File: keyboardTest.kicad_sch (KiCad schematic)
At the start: 4 parts, among them J1 COCO_CONNECTION, J1 DRAGON_CONNECTION

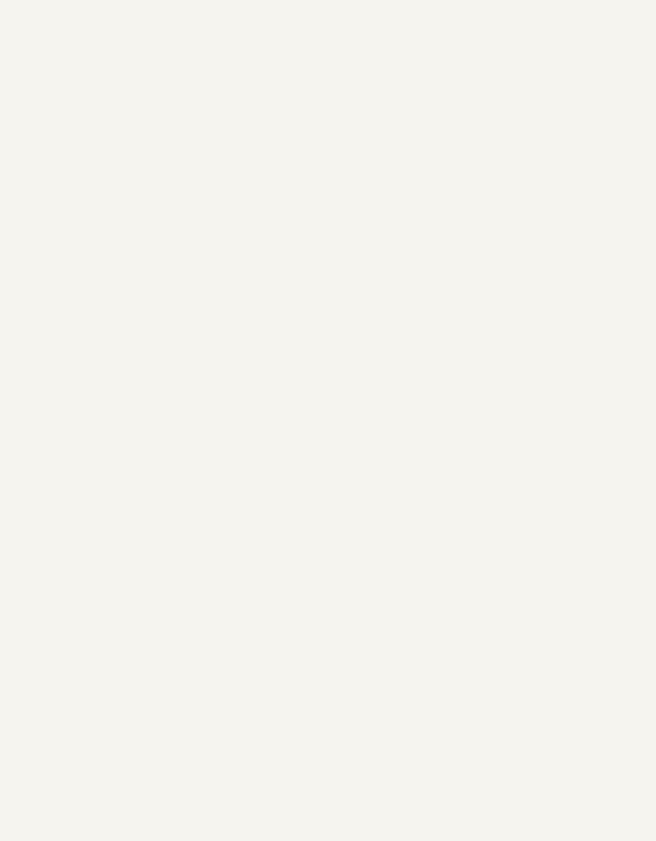
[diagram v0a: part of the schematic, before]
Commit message: add pico for hid
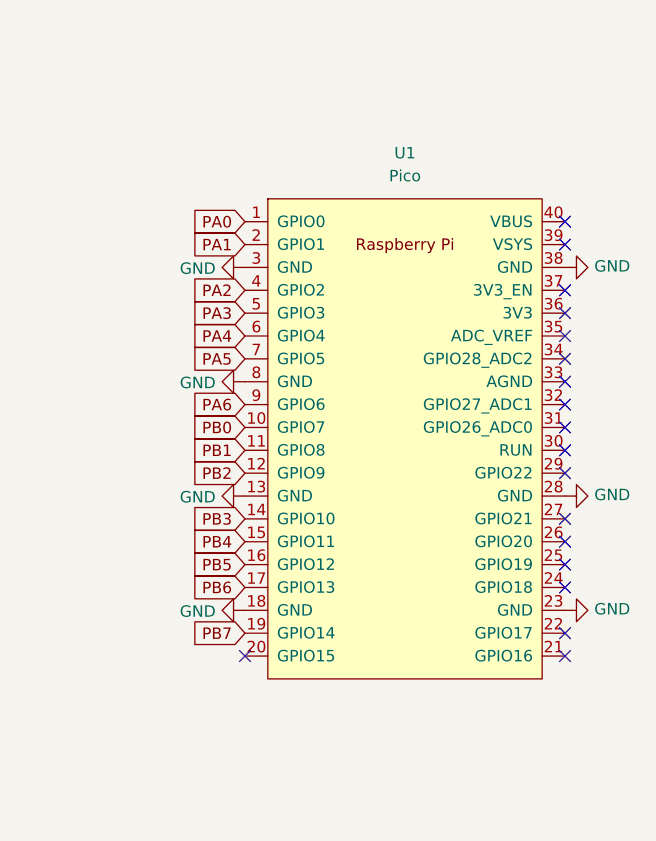
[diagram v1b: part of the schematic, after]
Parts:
- added U1: Pico, pico:RPi_Pico_SMD_TH, symbol pico:Pico
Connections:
- net GND: now also U1.13 (GND), U1.18 (GND), U1.23 (GND), U1.28 (GND), U1.3 (GND), U1.38 (GND), U1.8 (GND)
- net PA0: now also U1.1 (GPIO0)
- net PA1: now also U1.2 (GPIO1)
- net PA2: now also U1.4 (GPIO2)
- net PA3: now also U1.5 (GPIO3)
- net PA4: now also U1.6 (GPIO4)
- net PA5: now also U1.7 (GPIO5)
- net PA6: now also U1.9 (GPIO6)
- net PB0: now also U1.10 (GPIO7)
- net PB1: now also U1.11 (GPIO8)
- net PB2: now also U1.12 (GPIO9)
- net PB3: now also U1.14 (GPIO10)
- net PB4: now also U1.15 (GPIO11)
- net PB5: now also U1.16 (GPIO12)
- net PB6: now also U1.17 (GPIO13)
- net PB7: now also U1.19 (GPIO14)
- no-connect marks 0 -> 18

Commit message: update board mounting
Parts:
- added H10, H11, H3, H4, H5, H6, H7, H8, H9: MountingHole, MountingHole:MountingHole_3.2mm_M3, symbol Mechanical:MountingHole
- H1, H2: now left out of the parts list
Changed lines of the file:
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@@
+    )
+  )
+  (symbol (lib_id "Mechanical:MountingHole") (at 31.75 163.83 0) (unit 1)
+    (in_bom no) (on_board yes) (dnp yes) (fields_autoplaced)
+    (property "Reference" "H3" (at 34.29 163.195 0)
+      (effects (font (size 1.27 1.27)) (justify left))
+    )
+    (property "Value" "MountingHole" (at 34.29 165.735 0)
+      (effects (font (size 1.27 1.27)) (justify left))
+    )
+    (property "Footprint" "MountingHole:MountingHole_3.2mm_M3" (at 31.75 163.83 0)
+      (effects (font (size 1.27 1.27)) hide)
+    )
+    (property "Datasheet" "~" (at 31.75 163.83 0)
+      (effects (font (size 1.27 1.27)) hide)
+    )
+    (instances
+      (project "keyboardTest"
+        (path "/f35e9616-f481-4cdb-9e32-caf70bd322dd"
+          (reference "H3") (unit 1)
+        )
+      )
+    )
+  )
+  (symbol (lib_id "Mechanical:MountingHole") (at 60.96 178.562 0) (unit 1)
+    (in_bom no) (on_board yes) (dnp yes) (fields_autoplaced)
+    (property "Reference" "H6" (at 63.5 177.927 0)
+      (effects (font (size 1.27 1.27)) (justify left))
+    )
+    (property "Value" "MountingHole" (at 63.5 180.467 0)
+      (effects (font (size 1.27 1.27)) (justify left))
+    )
+    (property "Footprint" "MountingHole:MountingHole_3.2mm_M3" (at 60.96 178.562 0)
+      (effects (font (size 1.27 1.27)) hide)
+    )
+    (property "Datasheet" "~" (at 60.96 178.562 0)
+      (effects (font (size 1.27 1.27)) hide)
+    )
+    (instances
+      (project "keyboardTest"
+        (path "/f35e9616-f481-4cdb-9e32-caf70bd322dd"
+          (reference "H6") (unit 1)
+        )
+      )
+    )
+  )
+  (symbol (lib_id "Mechanical:MountingHole") (at 90.17 192.278 0) (unit 1)
+    (in_bom no) (on_board yes) (dnp yes) (fields_autoplaced)
+    (property "Reference" "H11" (at 92.71 191.643 0)
+      (effects (font (size 1.27 1.27)) (justify left))
+    )
+    (property "Value" "MountingHole" (at 92.71 194.183 0)
+      (effects (font (size 1.27 1.27)) (justify left))
+    )
+    (property "Footprint" "MountingHole:MountingHole_3.2mm_M3" (at 90.17 192.278 0)
+      (effects (font (size 1.27 1.27)) hide)
+    )
+    (property "Datasheet" "~" (at 90.17 192.278 0)
+      (effects (font (size 1.27 1.27)) hide)
+    )
+    (instances
+      (project "keyboardTest"
+        (path "/f35e9616-f481-4cdb-9e32-caf70bd322dd"
+          (reference "H11") (unit 1)
+        )
+      )
     )
   )
@@
         (path "/f35e9616-f481-4cdb-9e32-caf70bd322dd"
           (reference "#PWR03") (unit 1)
+        )
+      )
+    )
+  )
+  (symbol (lib_id "Mechanical:MountingHole") (at 32.766 177.546 0) (unit 1)
+    (in_bom no) (on_board yes) (dnp yes) (fields_autoplaced)
+    (property "Reference" "H4" (at 35.306 176.911 0)
+      (effects (font (size 1.27 1.27)) (justify left))
+    )
+    (property "Value" "MountingHole" (at 35.306 179.451 0)
+      (effects (font (size 1.27 1.27)) (justify left))
+    )
+    (property "Footprint" "MountingHole:MountingHole_3.2mm_M3" (at 32.766 177.546 0)
+      (effects (font (size 1.27 1.27)) hide)
+    )
+    (property "Datasheet" "~" (at 32.766 177.546 0)
+      (effects (font (size 1.27 1.27)) hide)
+    )
+    (instances
+      (project "keyboardTest"
+        (path "/f35e9616-f481-4cdb-9e32-caf70bd322dd"
+          (reference "H4") (unit 1)
         )
       )
@@
   )
   (symbol (lib_id "Mechanical:MountingHole") (at 59.69 132.588 0) (unit 1)
-    (in_bom yes) (on_board yes) (dnp no) (fields_autoplaced)
+    (in_bom no) (on_board yes) (dnp no) (fields_autoplaced)
     (property "Reference" "H1" (at 62.23 131.953 0)
       (effects (font (size 1.27 1.27)) (justify left))
@@
         (path "/f35e9616-f481-4cdb-9e32-caf70bd322dd"
           (reference "H1") (unit 1)
+        )
+      )
+    )
+  )
+  (symbol (lib_id "Mechanical:MountingHole") (at 89.3819 164.2902 0) (unit 1)
+    (in_bom no) (on_board yes) (dnp yes) (fields_autoplaced)
+    (property "Reference" "H9" (at 91.9219 163.6552 0)
+      (effects (font (size 1.27 1.27)) (justify left))
+    )
+    (property "Value" "MountingHole" (at 91.9219 166.1952 0)
+      (effects (font (size 1.27 1.27)) (justify left))
+    )
+    (property "Footprint" "MountingHole:MountingHole_3.2mm_M3" (at 89.3819 164.2902 0)
+      (effects (font (size 1.27 1.27)) hide)
+    )
+    (property "Datasheet" "~" (at 89.3819 164.2902 0)
+      (effects (font (size 1.27 1.27)) hide)
+    )
+    (instances
+      (project "keyboardTest"
+        (path "/f35e9616-f481-4cdb-9e32-caf70bd322dd"
+          (reference "H9") (unit 1)
+        )
+      )
+    )
+  )
+  (symbol (lib_id "Mechanical:MountingHole") (at 89.662 178.308 0) (unit 1)
+    (in_bom no) (on_board yes) (dnp yes) (fields_autoplaced)
+    (property "Reference" "H10" (at 92.202 177.673 0)
+      (effects (font (size 1.27 1.27)) (justify left))
+    )
+    (property "Value" "MountingHole" (at 92.202 180.213 0)
+      (effects (font (size 1.27 1.27)) (justify left))
+    )
+    (property "Footprint" "MountingHole:MountingHole_3.2mm_M3" (at 89.662 178.308 0)
+      (effects (font (size 1.27 1.27)) hide)
+    )
+    (property "Datasheet" "~" (at 89.662 178.308 0)
+      (effects (font (size 1.27 1.27)) hide)
+    )
+    (instances
+      (project "keyboardTest"
+        (path "/f35e9616-f481-4cdb-9e32-caf70bd322dd"
+          (reference "H10") (unit 1)
         )
       )
@@
     )
   )
+  (symbol (lib_id "Mechanical:MountingHole") (at 61.468 193.548 0) (unit 1)
+    (in_bom no) (on_board yes) (dnp yes) (fields_autoplaced)
+    (property "Reference" "H8" (at 64.008 192.913 0)
+      (effects (font (size 1.27 1.27)) (justify left))
+    )
+    (property "Value" "MountingHole" (at 64.008 195.453 0)
+      (effects (font (size 1.27 1.27)) (justify left))
+    )
+    (property "Footprint" "MountingHole:MountingHole_3.2mm_M3" (at 61.468 193.548 0)
+      (effects (font (size 1.27 1.27)) hide)
+    )
+    (property "Datasheet" "~" (at 61.468 193.548 0)
+      (effects (font (size 1.27 1.27)) hide)
+    )
+    (instances
+      (project "keyboardTest"
+        (path "/f35e9616-f481-4cdb-9e32-caf70bd322dd"
+          (reference "H8") (unit 1)
+        )
+      )
+    )
+  )
   (symbol (lib_id "power:GND") (at 199.39 106.68 90) (unit 1)
     (in_bom yes) (on_board yes) (dnp no)
@@
         (path "/f35e9616-f481-4cdb-9e32-caf70bd322dd"
           (reference "#PWR08") (unit 1)
+        )
+      )
+    )
+  )
+  (symbol (lib_id "Mechanical:MountingHole") (at 61.214 163.576 0) (unit 1)
+    (in_bom no) (on_board yes) (dnp yes) (fields_autoplaced)
+    (property "Reference" "H7" (at 63.754 162.941 0)
+      (effects (font (size 1.27 1.27)) (justify left))
+    )
+    (property "Value" "MountingHole" (at 63.754 165.481 0)
+      (effects (font (size 1.27 1.27)) (justify left))
+    )
+    (property "Footprint" "MountingHole:MountingHole_3.2mm_M3" (at 61.214 163.576 0)
+      (effects (font (size 1.27 1.27)) hide)
+    )
+    (property "Datasheet" "~" (at 61.214 163.576 0)
+      (effects (font (size 1.27 1.27)) hide)
+    )
+    (instances
+      (project "keyboardTest"
+        (path "/f35e9616-f481-4cdb-9e32-caf70bd322dd"
+          (reference "H7") (unit 1)
         )
       )
@@
   )
   (symbol (lib_id "Mechanical:MountingHole") (at 59.69 146.304 0) (unit 1)
-    (in_bom yes) (on_board yes) (dnp no) (fields_autoplaced)
+    (in_bom no) (on_board yes) (dnp no) (fields_autoplaced)
     (property "Reference" "H2" (at 62.23 145.669 0)
       (effects (font (size 1.27 1.27)) (justify left))
@@
         )
       )
+    )
+  )
+  (symbol (lib_id "Mechanical:MountingHole") (at 33.02 193.04 0) (unit 1)
+    (in_bom no) (on_board yes) (dnp yes) (fields_autoplaced)
+    (property "Reference" "H5" (at 35.56 192.405 0)
+      (effects (font (size 1.27 1.27)) (justify left))
+    )
+    (property "Value" "MountingHole" (at 35.56 194.945 0)
+      (effects (font (size 1.27 1.27)) (justify left))
+    )
+    (property "Footprint" "MountingHole:MountingHole_3.2mm_M3" (at 33.02 193.04 0)
+      (effects (font (size 1.27 1.27)) hide)
+    )
+    (property "Datasheet" "~" (at 33.02 193.04 0)
+      (effects (font (size 1.27 1.27)) hide)
+    )
+    (instances
+      (project "keyboardTest"
+        (path "/f35e9616-f481-4cdb-9e32-caf70bd322dd"
+          (reference "H5") (unit 1)
+        )
+      )

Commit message: reshape board for fit
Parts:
- H1, H2: footprint MountingHole:MountingHole_5.3mm_M5 -> MountingHole:MountingHole_5.3mm_M5_ISO7380_Pad
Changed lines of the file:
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@@
       (effects (font (size 1.27 1.27)) (justify left))
     )
-    (property "Footprint" "MountingHole:MountingHole_5.3mm_M5" (at 59.69 132.588 0)
+    (property "Footprint" "MountingHole:MountingHole_5.3mm_M5_ISO7380_Pad" (at 59.69 132.588 0)
       (effects (font (size 1.27 1.27)) hide)
     )
@@
       (effects (font (size 1.27 1.27)) (justify left))
     )
-    (property "Footprint" "MountingHole:MountingHole_5.3mm_M5" (at 59.69 146.304 0)
-      (effects (font (size 1.27 1.27)) hide)
-    )
+    (property "Footprint" "MountingHole:MountingHole_5.3mm_M5_ISO7380_Pad" (at 59.69 146.304 0)
+      (effects (font (size 1.27 1.27)) hide)
+    )
